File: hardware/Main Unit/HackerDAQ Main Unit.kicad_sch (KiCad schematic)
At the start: 5 parts, among them X2 8.192MHz

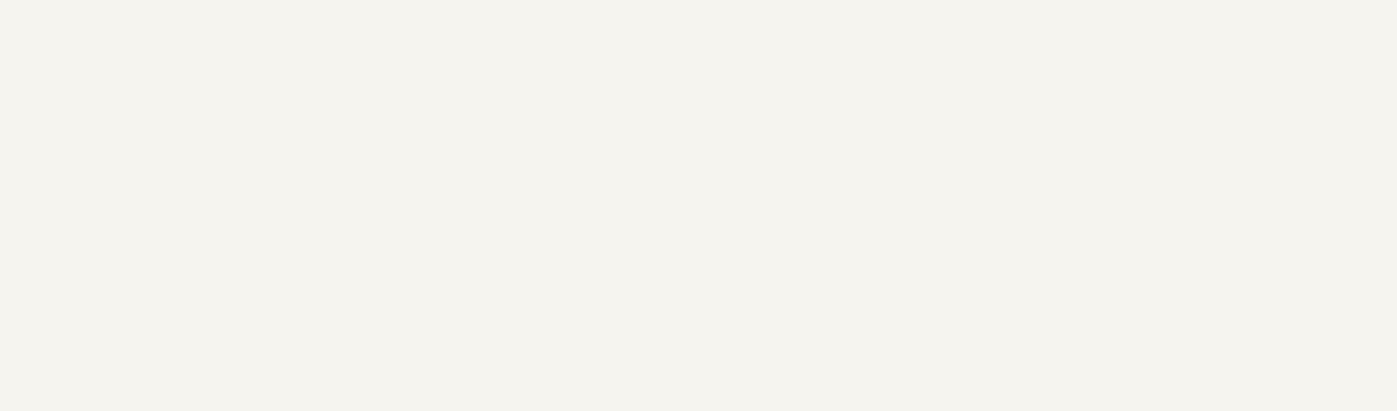
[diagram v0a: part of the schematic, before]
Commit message: Add Main Unit to CI build as well
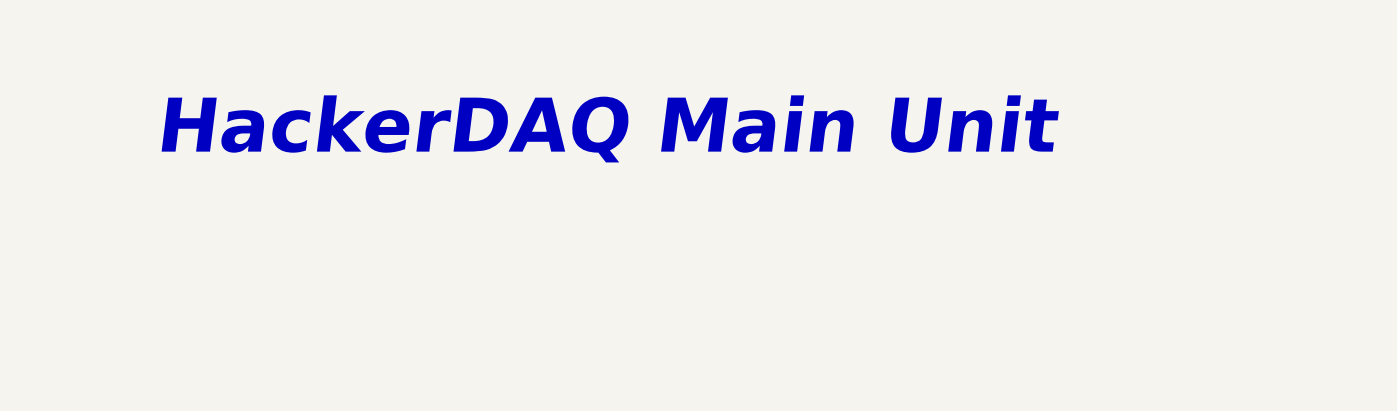
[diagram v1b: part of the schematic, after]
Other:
- note added: "HackerDAQ Main Unit"
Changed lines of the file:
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@@
 		)
 	)
+	(text "HackerDAQ Main Unit"
+		(exclude_from_sim no)
+		(at 27.432 32.512 0)
+		(effects
+			(font
+				(face "Calibri")
+				(size 6 6)
+				(thickness 0.8)
+				(bold yes)
+				(italic yes)
+			)
+			(justify left bottom)
+		)
+	)
 	(text "Main 3.3V Supply"
 		(exclude_from_sim no)
@@
 		)
 		(instances
-			(project "Main Unit"
+			(project "HackerDAQ Main Unit"
 				(path "/7d91f165-331a-4c48-9d02-ee2a0aa7e94a"
 					(page "8")
@@
 		)
 		(instances
-			(project "Main Unit"
+			(project "HackerDAQ Main Unit"
 				(path "/7d91f165-331a-4c48-9d02-ee2a0aa7e94a"
 					(page "8")
@@
 		)
 		(instances
-			(project "Main Unit"
+			(project "HackerDAQ Main Unit"
 				(path "/7d91f165-331a-4c48-9d02-ee2a0aa7e94a"
 					(page "10")
@@
 		)
 		(instances
-			(project "Main Unit"
+			(project "HackerDAQ Main Unit"
 				(path "/7d91f165-331a-4c48-9d02-ee2a0aa7e94a"
 					(page "4")
@@
 		)
 		(instances
-			(project "Main Unit"
+			(project "HackerDAQ Main Unit"
 				(path "/7d91f165-331a-4c48-9d02-ee2a0aa7e94a"
 					(page "7")
@@
 		)
 		(instances
-			(project "Main Unit"
+			(project "HackerDAQ Main Unit"
 				(path "/7d91f165-331a-4c48-9d02-ee2a0aa7e94a"
 					(page "12")
@@
 		)
 		(instances
-			(project "Main Unit"
+			(project "HackerDAQ Main Unit"
 				(path "/7d91f165-331a-4c48-9d02-ee2a0aa7e94a"
 					(page "6")
@@
 		)
 		(instances
-			(project "Main Unit"
+			(project "HackerDAQ Main Unit"
 				(path "/7d91f165-331a-4c48-9d02-ee2a0aa7e94a"
 					(page "5")
@@
 		)
 		(instances
-			(project "Main Unit"
+			(project "HackerDAQ Main Unit"
 				(path "/7d91f165-331a-4c48-9d02-ee2a0aa7e94a"
 					(page "11")
@@
 		)
 		(instances
-			(project "Main Unit"
+			(project "HackerDAQ Main Unit"
 				(path "/7d91f165-331a-4c48-9d02-ee2a0aa7e94a"
 					(page "9")
@@
 		)
 		(instances
-			(project "Main Unit"
+			(project "HackerDAQ Main Unit"
 				(path "/7d91f165-331a-4c48-9d02-ee2a0aa7e94a"
 					(page "2")

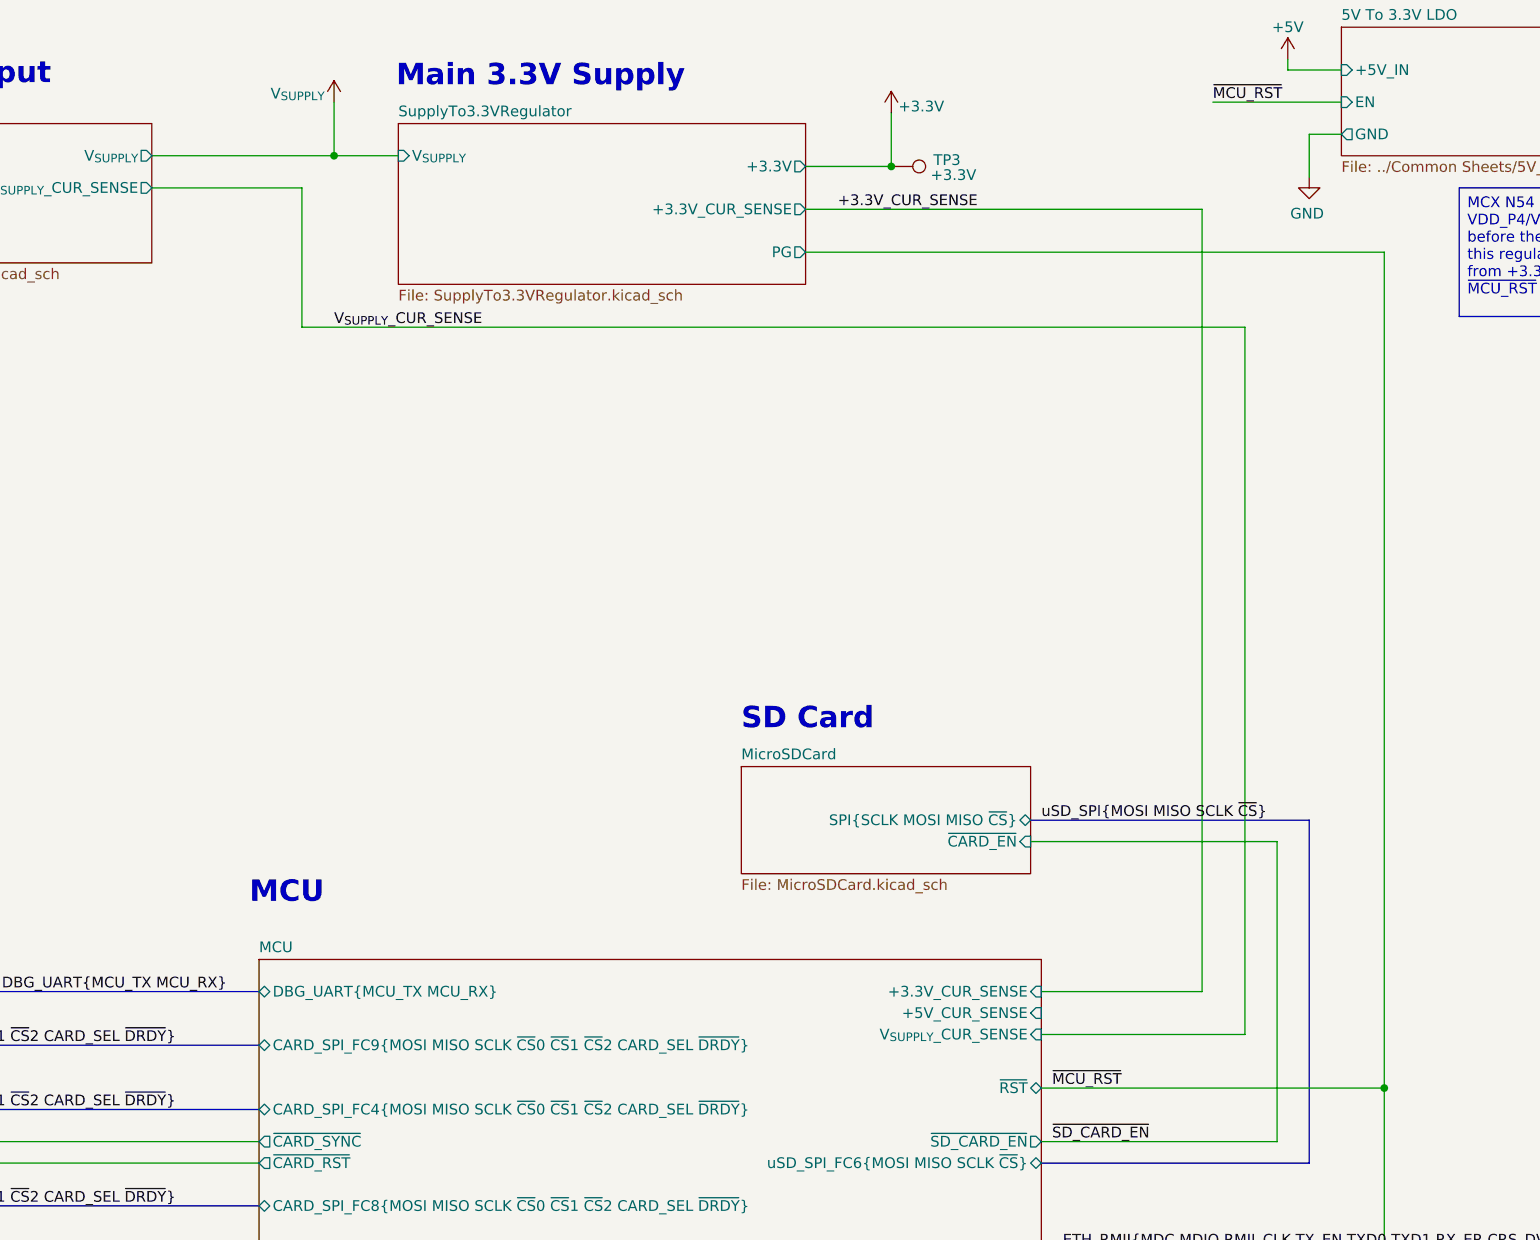
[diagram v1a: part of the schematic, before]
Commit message: Add LEDs and 5V regulator to main unit
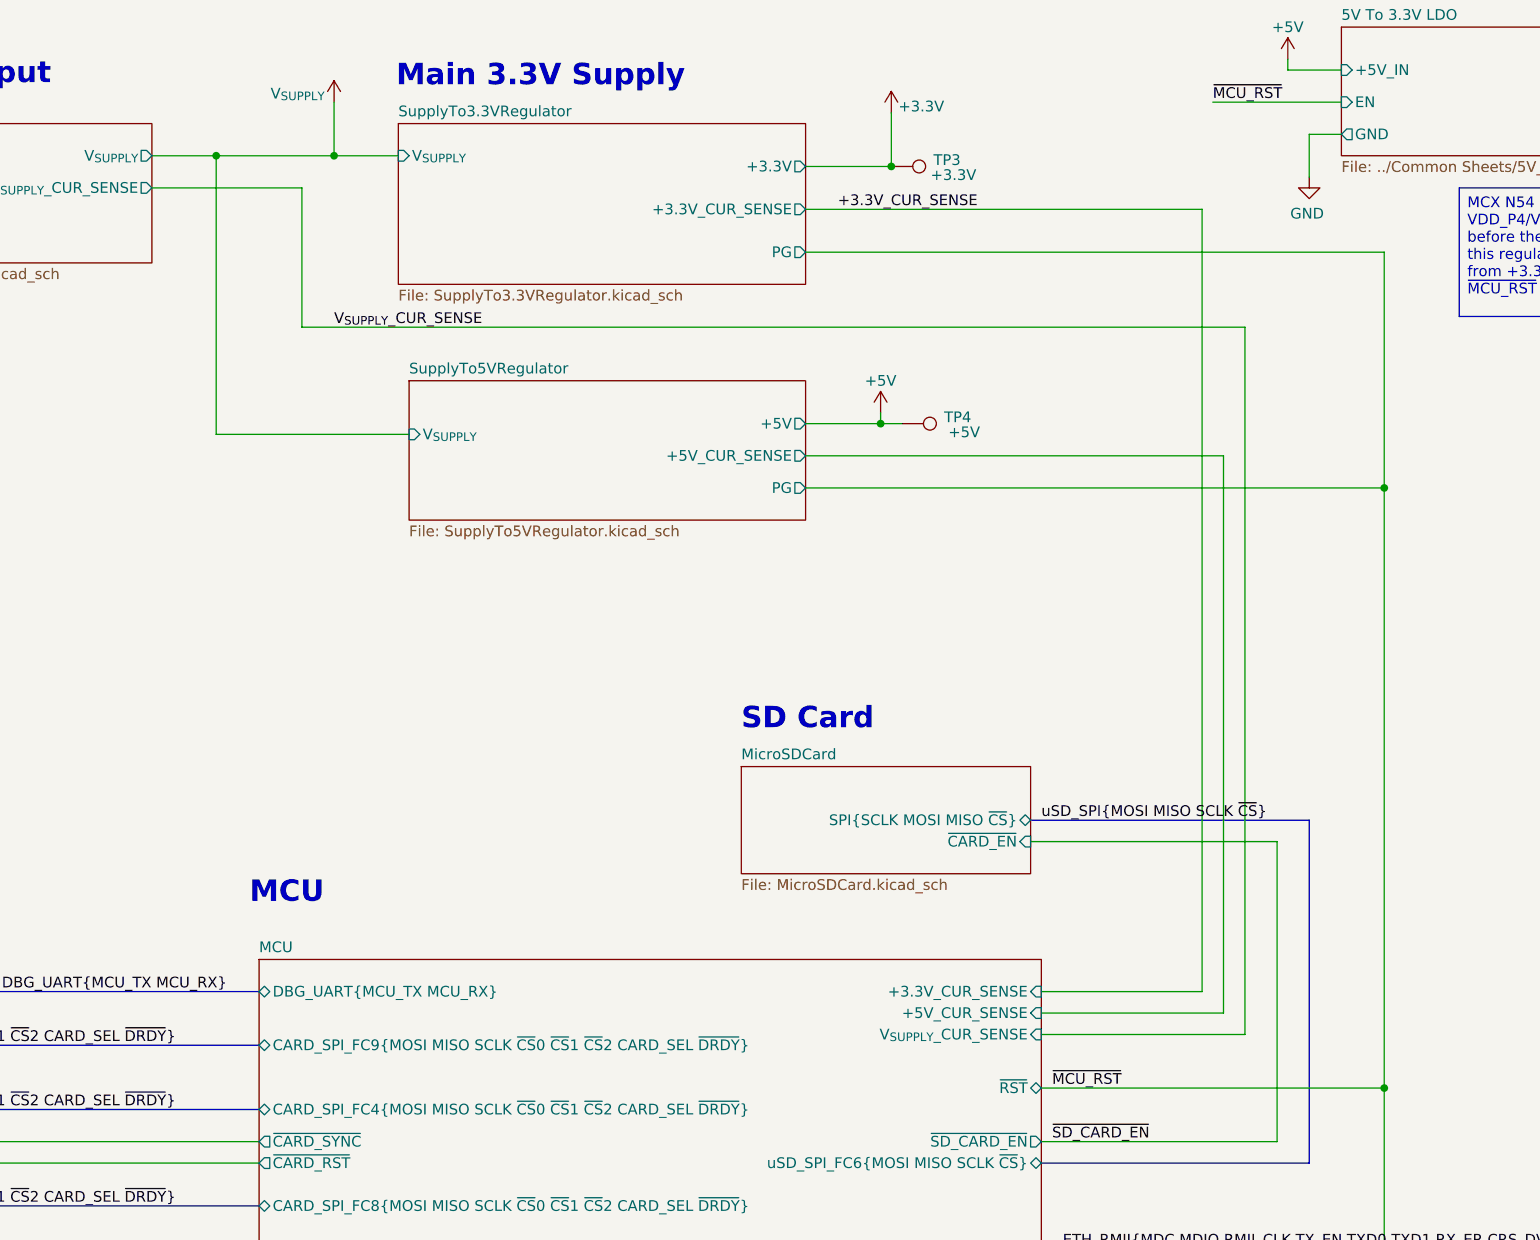
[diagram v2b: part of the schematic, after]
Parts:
- added TP4: +5V, TestPoint:TestPoint_THTPad_D2.5mm_Drill1.2mm, symbol Connector:TestPoint
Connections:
- net +5V: now also TP4.1
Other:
- added sheet SupplyTo5VRegulator (SupplyTo5VRegulator.kicad_sch)

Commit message: Main board routed!!
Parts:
- added H1, H2, H3, H4: MountingHole_Pad, MountingHole:MountingHole_4.3mm_M4_DIN965_Pad, symbol Mechanical:MountingHole_Pad
- X2: footprint Oscillator:Oscillator_SMD_ECS_2520MV-xxx-xx-4Pin_2.5x2.0mm -> Project Library:Oscillator_SMD_ECS_2520MV-xxx-xx-4Pin_2.5x2.0mm_Fixed3DModel
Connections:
- net GND: now also H1.1, H2.1, H3.1, H4.1
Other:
- note added: "Main 5V Supply"
- moved on the sheet: TP4

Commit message: Geographical reannotate
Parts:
- renumbered C52 to C21, H4 to H1, H1 to H4, TP2 to TP1, TP4 to TP3, TP3 to TP4
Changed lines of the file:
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@@
 		(on_board yes)
 		(dnp no)
-		(property "Reference" "H4"
+		(property "Reference" "H1"
 			(at 262.89 263.398 0)
 			(effects
@@
 			(project "HackerDAQ Main Unit"
 				(path "/7d91f165-331a-4c48-9d02-ee2a0aa7e94a"
-					(reference "H4")
+					(reference "H1")
 					(unit 1)
 				)
@@
 		(on_board yes)
 		(dnp no)
-		(property "Reference" "TP2"
+		(property "Reference" "TP1"
 			(at 400.812 34.036 0)
 			(effects
@@
 			(project "HackerDAQ Main Unit"
 				(path "/7d91f165-331a-4c48-9d02-ee2a0aa7e94a"
-					(reference "TP2")
+					(reference "TP1")
 					(unit 1)
 				)
@@
 		(on_board yes)
 		(dnp no)
-		(property "Reference" "TP3"
+		(property "Reference" "TP4"
 			(at 305.054 41.148 90)
 			(effects
@@
 			(project "HackerDAQ Main Unit"
 				(path "/7d91f165-331a-4c48-9d02-ee2a0aa7e94a"
-					(reference "TP3")
+					(reference "TP4")
 					(unit 1)
 				)
@@
 		(on_board yes)
 		(dnp no)
-		(property "Reference" "TP4"
+		(property "Reference" "TP3"
 			(at 306.324 76.708 90)
 			(effects
@@
 			(project "HackerDAQ Main Unit"
 				(path "/7d91f165-331a-4c48-9d02-ee2a0aa7e94a"
-					(reference "TP4")
+					(reference "TP3")
 					(unit 1)
 				)
@@
 		(dnp no)
 		(fields_autoplaced yes)
-		(property "Reference" "C52"
+		(property "Reference" "C21"
 			(at 71.12 246.3862 0)
 			(effects
@@
 			(project "HackerDAQ Main Unit"
 				(path "/7d91f165-331a-4c48-9d02-ee2a0aa7e94a"
-					(reference "C52")
+					(reference "C21")
 					(unit 1)
 				)
@@
 		(on_board yes)
 		(dnp no)
-		(property "Reference" "H1"
+		(property "Reference" "H4"
 			(at 247.65 263.398 0)
 			(effects
@@
 			(project "HackerDAQ Main Unit"
 				(path "/7d91f165-331a-4c48-9d02-ee2a0aa7e94a"
-					(reference "H1")
-					(unit 1)
-				)
+					(reference "H4")
+					(unit 1)
+				)
